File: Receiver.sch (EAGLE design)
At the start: 11 parts, among them IC1 25LC080P, J1 PIC_ICSP_6_PIN, U1 915MHz, U2 DS3234, X1 BU-SMA-V

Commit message: Updates
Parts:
- added BUTTON: TSW-106-02-S-S, con-samtec:TSW-106-02-S-S
- added C3, C4: (no value), resistor:C-EU050-025X075
- added PWR: 22-27-2021-02, con-molex:22-27-2021-02
- added SJ1: SOLDERJUMPERNO, SparkFun-Retired:SOLDERJUMPERNO
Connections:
- net N$10 renamed MOSI1
- net N$11 renamed MOSI2
- net N$6 renamed SCK1
- net N$7 renamed MISO1
- net N$8 renamed SCK2
- net N$9 renamed MISO2
- new net N$10: BUTTON-4.1, U$1.RD0
- new net N$11: BUTTON-6.1, U$1.RD3
- new net N$17: RA8875-8.S, U$1.RA4
- new net N$18: RA8875-4.S, U$1.RA0
- new net N$19: RA8875-10.S, U$1.RE1
- new net N$20: RA8875-11.S, U$1.RE2
- new net N$21: U$1.RD7, U1.DIO0
- new net N$22: J1.VCC, SJ1.1
- new net N$6: BUTTON-1.1, U$1.RC0
- new net N$7: BUTTON-2.1, U$1.RC1
- new net N$8: BUTTON-3.1, U$1.RC2
- new net N$9: BUTTON-5.1, U$1.RD1
- net +3V3: now also C3.1, C4.1, PWR-1.S, RA8875-1.S, SJ1.2; no longer J1.VCC
- net GND: now also C3.2, C4.2, PWR-2.S
- net N$12: now also U$1.RD6; no longer U$1.RD3
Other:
- moved on the sheet: BT1, IC1, U2

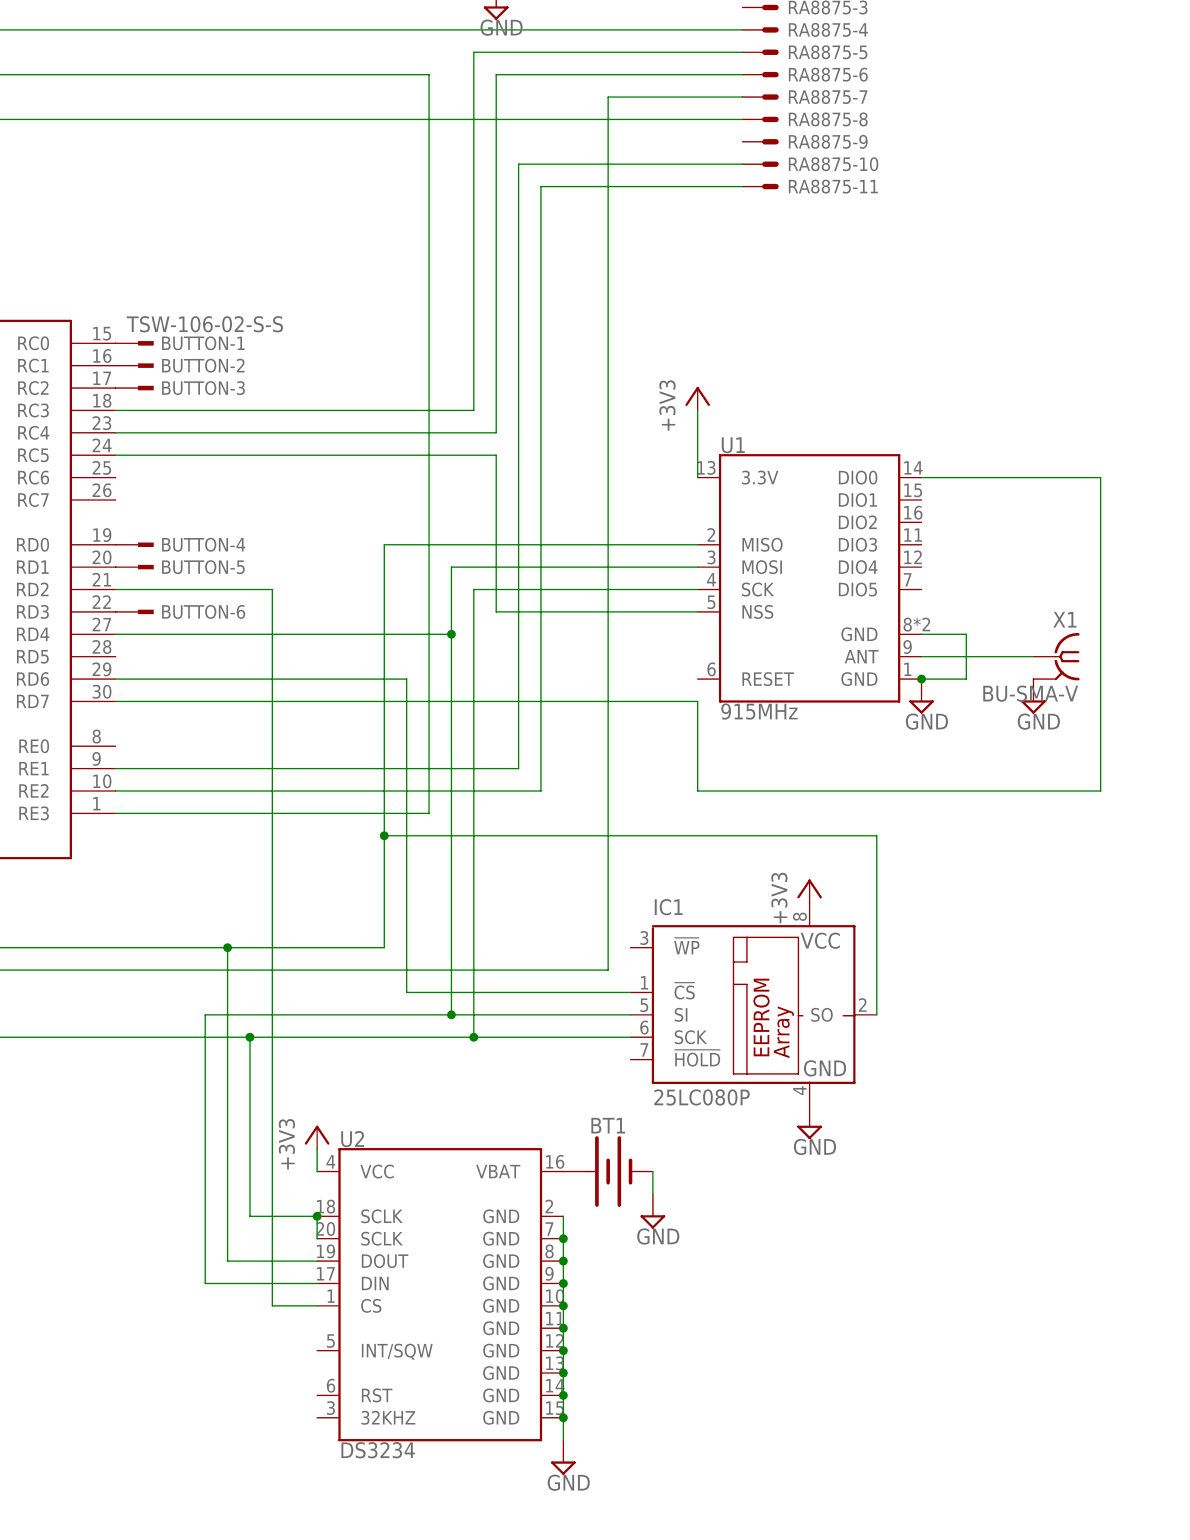
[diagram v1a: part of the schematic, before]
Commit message: Ordered sender PCB
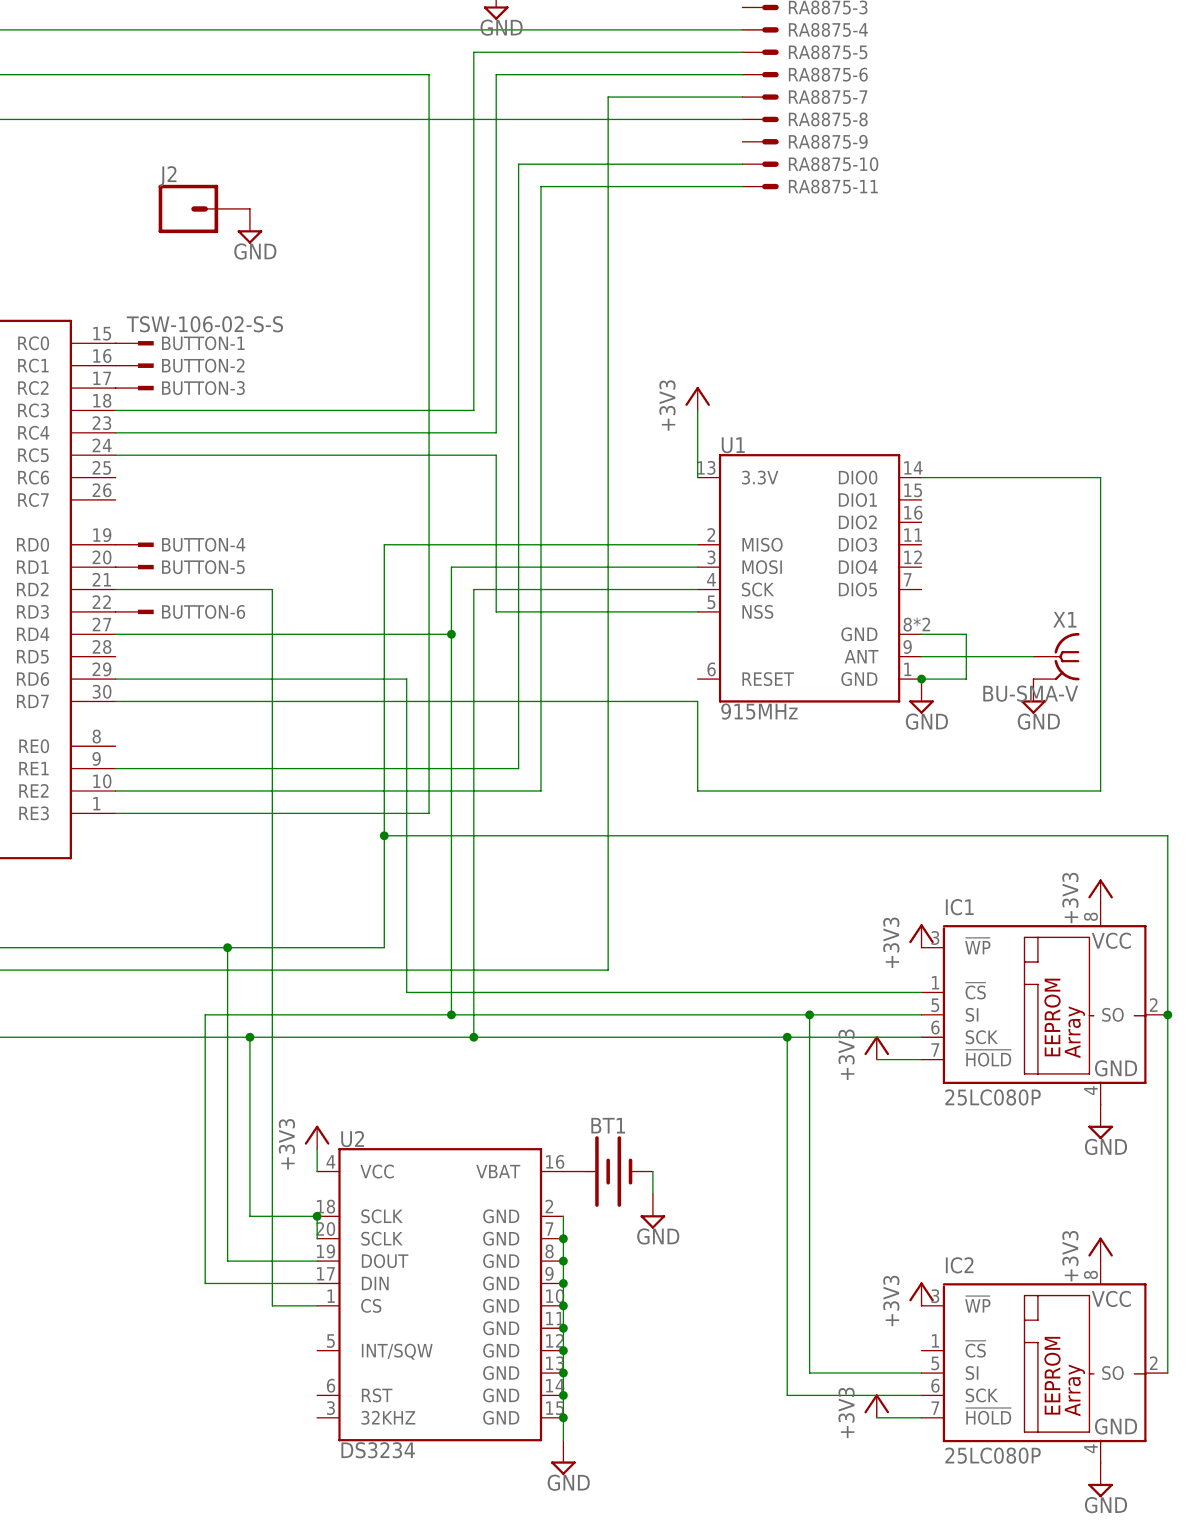
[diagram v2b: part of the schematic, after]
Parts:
- added IC2: 25LC080P, microchip:25LC080P
- added J2: (no value), SparkFun-Connectors:CONN_01
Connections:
- net +3V3: now also IC1.!HOLD, IC1.!WP, IC2.!HOLD, IC2.!WP, IC2.VCC
- net GND: now also IC2.GND, J2.1
- net MISO2: now also IC2.SO
- net MOSI2: now also IC2.SI
- net SCK2: now also IC2.SCK
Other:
- moved on the sheet: IC1
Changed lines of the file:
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@@
 <part name="C3" library="resistor" deviceset="C-EU" device="050-025X075"/>
 <part name="C4" library="resistor" deviceset="C-EU" device="050-025X075"/>
+<part name="IC2" library="microchip" deviceset="25*" device="P" technology="LC080"/>
+<part name="+3V8" library="supply1" deviceset="+3V3" device=""/>
+<part name="SUPPLY3" library="supply2" deviceset="GND" device=""/>
+<part name="+3V9" library="supply1" deviceset="+3V3" device=""/>
+<part name="+3V10" library="supply1" deviceset="+3V3" device=""/>
+<part name="+3V11" library="supply1" deviceset="+3V3" device=""/>
+<part name="+3V12" library="supply1" deviceset="+3V3" device=""/>
+<part name="J2" library="SparkFun-Connectors" deviceset="CONN_01" device=""/>
+<part name="SUPPLY6" library="supply2" deviceset="GND" device=""/>
 </parts>
 <sheets>
@@
 <instance part="RA8875" gate="-10" x="172.72" y="121.92"/>
 <instance part="RA8875" gate="-11" x="172.72" y="119.38"/>
-<instance part="IC1" gate="G$1" x="170.18" y="25.4"/>
-<instance part="SUPPLY7" gate="GND" x="177.8" y="12.7"/>
+<instance part="IC1" gate="G$1" x="203.2" y="25.4"/>
+<instance part="SUPPLY7" gate="GND" x="210.82" y="12.7"/>
 <instance part="SUPPLY8" gate="GND" x="190.5" y="60.96"/>
 <instance part="X1" gate="G$1" x="205.74" y="66.04" rot="MR0"/>
@@
 <instance part="+3V3" gate="G$1" x="78.74" y="111.76"/>
 <instance part="+3V4" gate="G$1" x="50.8" y="121.92"/>
-<instance part="+3V5" gate="G$1" x="177.8" y="40.64"/>
+<instance part="+3V5" gate="G$1" x="210.82" y="40.64"/>
 <instance part="+3V6" gate="G$1" x="162.56" y="147.32"/>
 <instance part="BUTTON" gate="-1" x="101.6" y="101.6"/>
@@
 <instance part="C3" gate="G$1" x="7.62" y="149.86"/>
 <instance part="C4" gate="G$1" x="-7.62" y="149.86"/>
+<instance part="IC2" gate="G$1" x="203.2" y="-15.24"/>
+<instance part="+3V8" gate="G$1" x="210.82" y="0"/>
+<instance part="SUPPLY3" gate="GND" x="210.82" y="-27.94"/>
+<instance part="+3V9" gate="G$1" x="190.5" y="35.56"/>
+<instance part="+3V10" gate="G$1" x="190.5" y="-5.08"/>
+<instance part="+3V11" gate="G$1" x="185.42" y="-17.78"/>
+<instance part="+3V12" gate="G$1" x="185.42" y="22.86"/>
+<instance part="J2" gate="G$1" x="106.68" y="116.84"/>
+<instance part="SUPPLY6" gate="GND" x="114.3" y="114.3"/>
 </instances>
 <busses>
@@
 <junction x="7.62" y="144.78"/>
 </segment>
+<segment>
+<pinref part="IC2" gate="G$1" pin="GND"/>
+<pinref part="SUPPLY3" gate="GND" pin="GND"/>
+</segment>
+<segment>
+<pinref part="J2" gate="G$1" pin="1"/>
+<pinref part="SUPPLY6" gate="GND" pin="GND"/>
+</segment>
 </net>
 <net name="N$1" class="0">
@@
 <wire x1="129.54" y1="78.74" x2="165.1" y2="78.74" width="0.1524" layer="91"/>
 <pinref part="IC1" gate="G$1" pin="SO"/>
-<wire x1="185.42" y1="25.4" x2="185.42" y2="45.72" width="0.1524" layer="91"/>
-<wire x1="185.42" y1="45.72" x2="129.54" y2="45.72" width="0.1524" layer="91"/>
+<wire x1="218.44" y1="25.4" x2="218.44" y2="45.72" width="0.1524" layer="91"/>
+<wire x1="218.44" y1="45.72" x2="129.54" y2="45.72" width="0.1524" layer="91"/>
 <junction x="129.54" y="45.72"/>
 <pinref part="U2" gate="G$1" pin="DOUT"/>
@@
 <wire x1="111.76" y1="-2.54" x2="111.76" y2="33.02" width="0.1524" layer="91"/>
 <junction x="111.76" y="33.02"/>
+<pinref part="IC2" gate="G$1" pin="SO"/>
+<wire x1="218.44" y1="25.4" x2="218.44" y2="-15.24" width="0.1524" layer="91"/>
+<junction x="218.44" y="25.4"/>
 </segment>
 </net>
@@
 <segment>
 <pinref part="IC1" gate="G$1" pin="SI"/>
-<wire x1="157.48" y1="25.4" x2="137.16" y2="25.4" width="0.1524" layer="91"/>
+<wire x1="190.5" y1="25.4" x2="177.8" y2="25.4" width="0.1524" layer="91"/>
 <pinref part="U1" gate="G$1" pin="MOSI"/>
+<wire x1="177.8" y1="25.4" x2="137.16" y2="25.4" width="0.1524" layer="91"/>
 <wire x1="137.16" y1="25.4" x2="137.16" y2="68.58" width="0.1524" layer="91"/>
 <wire x1="137.16" y1="68.58" x2="137.16" y2="76.2" width="0.1524" layer="91"/>
@@
 <wire x1="99.06" y1="68.58" x2="137.16" y2="68.58" width="0.1524" layer="91"/>
 <junction x="137.16" y="68.58"/>
+<wire x1="177.8" y1="25.4" x2="177.8" y2="-15.24" width="0.1524" layer="91"/>
+<junction x="177.8" y="25.4"/>
+<pinref part="IC2" gate="G$1" pin="SI"/>
+<wire x1="177.8" y1="-15.24" x2="190.5" y2="-15.24" width="0.1524" layer="91"/>
 </segment>
 </net>
@@
 <pinref part="SJ1" gate="1" pin="2"/>
 <wire x1="50.8" y1="119.38" x2="45.72" y2="119.38" width="0.1524" layer="91"/>
+</segment>
+<segment>
+<pinref part="IC2" gate="G$1" pin="VCC"/>
+<pinref part="+3V8" gate="G$1" pin="+3V3"/>
+</segment>
+<segment>
+<pinref part="IC1" gate="G$1" pin="!WP"/>
+<pinref part="+3V9" gate="G$1" pin="+3V3"/>
+</segment>
+<segment>
+<pinref part="IC2" gate="G$1" pin="!WP"/>
+<pinref part="+3V10" gate="G$1" pin="+3V3"/>
+</segment>
+<segment>
+<pinref part="IC1" gate="G$1" pin="!HOLD"/>
+<pinref part="+3V12" gate="G$1" pin="+3V3"/>
+<wire x1="190.5" y1="20.32" x2="185.42" y2="20.32" width="0.1524" layer="91"/>
+</segment>
+<segment>
+<pinref part="IC2" gate="G$1" pin="!HOLD"/>
+<pinref part="+3V11" gate="G$1" pin="+3V3"/>
+<wire x1="190.5" y1="-20.32" x2="185.42" y2="-20.32" width="0.1524" layer="91"/>
 </segment>
 </net>
@@
 <pinref part="U1" gate="G$1" pin="SCK"/>
 <wire x1="114.3" y1="22.86" x2="139.7" y2="22.86" width="0.1524" layer="91"/>
-<wire x1="139.7" y1="22.86" x2="157.48" y2="22.86" width="0.1524" layer="91"/>
+<wire x1="139.7" y1="22.86" x2="175.26" y2="22.86" width="0.1524" layer="91"/>
+<wire x1="175.26" y1="22.86" x2="190.5" y2="22.86" width="0.1524" layer="91"/>
 <wire x1="165.1" y1="73.66" x2="139.7" y2="73.66" width="0.1524" layer="91"/>
 <wire x1="139.7" y1="73.66" x2="139.7" y2="22.86" width="0.1524" layer="91"/>
@@
 <junction x="121.92" y="2.54"/>
 <junction x="114.3" y="22.86"/>
+<wire x1="175.26" y1="22.86" x2="175.26" y2="-17.78" width="0.1524" layer="91"/>
+<junction x="175.26" y="22.86"/>
+<pinref part="IC2" gate="G$1" pin="SCK"/>
+<wire x1="175.26" y1="-17.78" x2="190.5" y2="-17.78" width="0.1524" layer="91"/>
 </segment>
 </net>
@@
 <pinref part="IC1" gate="G$1" pin="!CS"/>
 <wire x1="132.08" y1="63.5" x2="132.08" y2="27.94" width="0.1524" layer="91"/>
-<wire x1="132.08" y1="27.94" x2="157.48" y2="27.94" width="0.1524" layer="91"/>
+<wire x1="132.08" y1="27.94" x2="190.5" y2="27.94" width="0.1524" layer="91"/>
 <pinref part="U$1" gate="G$1" pin="RD6"/>
 <wire x1="99.06" y1="63.5" x2="132.08" y2="63.5" width="0.1524" layer="91"/>

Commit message: Updated receiver PCB
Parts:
- removed J1: PIC_ICSP_6_PIN, SparkFun-Connectors:PIC_ICSP_6_PIN
- added IC3: (no value), v-reg:78XXS
- added PWR1: 22-27-2021-02, con-molex:22-27-2021-02
- added R1, R2, R3, R4, R5, R6: (no value), resistor:R-US_M1206
- added X2: 53047-05, con-molex:53047-05
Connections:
- new net N$23: IC2.!CS, U$1.RC6
- new net N$24: IC3.IN, PWR1-1.S
- net +3V3: now also IC3.OUT, R1.2, R2.2, R3.2, R4.2, R5.2, R6.2
- net GND: now also IC3.GND, PWR1-2.S, X2-3.S; no longer J1.GND
- net N$1: now also X2-4.S; no longer J1.PGD
- net N$10: now also R4.1
- net N$11: now also R6.1
- net N$2: now also X2-5.S; no longer J1.PGC
- net N$22: now also X2-2.S; no longer J1.VCC
- net N$3: now also X2-1.S; no longer J1.VPP
- net N$6: now also R1.1
- net N$7: now also R2.1
- net N$8: now also R3.1
- net N$9: now also R5.1
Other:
- moved on the sheet: BUTTON-1, BUTTON-2, BUTTON-3, BUTTON-4, BUTTON-5, BUTTON-6

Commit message: Receiver board r2
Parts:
- removed BT1: (no value), SparkFun-Batteries:BATTERY-20MM_SMD
- removed BUTTON: TSW-106-02-S-S, con-samtec:TSW-106-02-S-S
- removed IC1, IC2: 25LC080P, microchip:25LC080P
- removed IC3: (no value), v-reg:78XXS
- removed PWR1: 22-27-2021-02, con-molex:22-27-2021-02
- removed Q1: (no value), crystal:CRYSTALHC49U-V
- removed R2, R3, R4, R5, R6: (no value), resistor:R-US_M1206
- removed SJ1: SOLDERJUMPERNO, SparkFun-Retired:SOLDERJUMPERNO
- removed U$1: PIC18F47K40, microchip:PIC18F47K40
- added C5, C6: (no value), resistor:C-EUC1206
- added C7: 0.1uF, resistor:C-EUC1206
- added I2C-DBG: (no value), SparkFun-Connectors:CONN_03
- added J1: SD_CARD_SOCKET, SparkFun-Connectors:SD_CARD_SOCKET
- added RA8875-DBG: (no value), SparkFun-Connectors:CONN_09
- added SPI2-DBG: (no value), SparkFun-Connectors:CONN_08"
- added TP3V3, TPCLKOUT, TPSQW, TPVBUS: TPB2,54, testpad:TPB2,54
- added U$3: (no value), adafruit:CR1220SMT
- added U4: FT232RL, SparkFun-IC-Comms:FT232RL-BASICSSOP
- added U5: DS1374C, FRC696:DS1374C
- added U6: +12v, SparkFun-IC-Power:V_REG_78XX7812
- added UARTDBG: 53047-03, con-molex:53047-03
- C1: value (none) -> 0.1uF
- C2: value (none) -> 1uF
- C3: value (none) -> 0.1uF; device resistor:C-EU050-025X075 -> resistor:C-EUC1206
- C4: value (none) -> 1uF; device resistor:C-EU050-025X075 -> resistor:C-EUC1206
- J2: device SparkFun-Connectors:CONN_01 -> SparkFun-Connectors:USB_MICRO-B_FEMALE-SMT
- PWR: value 22-27-2021-02 -> 53261-02; device con-molex:22-27-2021-02 -> con-molex:53261-02
- R1: value (none) -> 10k; device resistor:R-US_M1206 -> resistor:R-US_R1206
- RA8875: value C-GRID-11-70543 -> C-GRID-10-70543; device con-molex:C-GRID-11-70543 -> con-molex:C-GRID-10-70543
- U1: value 915MHz -> PIC18F47Q84; device SparkFun-RF:RFM69HCW-915 -> FRC696:PIC18F47Q84
- U2: value DS3234 -> 915MHz; device SparkFun-Clocks:DS3234 -> SparkFun-RF:RFM69HCW-915
- X2: value 53047-05 -> PIC-PROG047; device con-molex:53047-05 -> FRC696:PIC-PROG047
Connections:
- removed net N$14: BT1.+, U2.VBAT
- removed net N$15: U$1.RC5, U1.NSS
- removed net N$16: U$1.RD2, U2.CS
- removed net N$17: RA8875-8.S, U$1.RA4
- removed net N$18: RA8875-4.S, U$1.RA0
- removed net N$19: RA8875-10.S, U$1.RE1
- removed net N$20: RA8875-11.S, U$1.RE2
- removed net N$21: U$1.RD7, U1.DIO0
- removed net N$22: SJ1.1, X2-2.S
- removed net N$23: IC2.!CS, U$1.RC6
- removed net N$24: IC3.IN, PWR1-1.S
- new net CLK_RST: U5.!RST
- new net RA8875-CS: RA8875-7.S, RA8875-DBG.6, U1.RD7
- new net RA8875-INT: RA8875-10.S, RA8875-DBG.9, U1.RC4
- new net RA8875-LITE: RA8875-3.S, RA8875-DBG.2, U1.RD0
- new net RA8875-RST: RA8875-8.S, RA8875-DBG.7, U1.RD6
- new net RA8875-WAIT: RA8875-9.S, RA8875-DBG.8, U1.RD5
- new net RF-CS: SPI2-DBG.5, U1.RC5, U2.NSS
- new net RF-DIO0: SPI2-DBG.7, U1.RC7, U2.DIO0
- new net RF-RST: SPI2-DBG.6, U1.RC6, U2.RESET
- new net SCL: I2C-DBG.2, U1.RB5, U5.SCL
- new net SD-CS: J1.CD/DAT3, SPI2-DBG.8, U1.RD4
- new net SDA: I2C-DBG.3, U1.RB4, U5.SDA
- new net UARTRX: U1.RB2, U4.TXD, UARTDBG-3.S
- new net UARTTX: U1.RB1, U4.RXD, UARTDBG-2.S
- net +3V3: now also C5.1, C6.1, J1.VDD, TP3V3.TP, U1.VDD@1, U1.VDD@2, U2.3.3V, U4.VCC, U4.VCCIO, U5.VCC, U6.OUT, X2VDD.S; no longer IC1.!HOLD, IC1.!WP, IC1.VCC, IC2.!HOLD, IC2.!WP, IC2.VCC, IC3.OUT, PWR-1.S, R2.2, R3.2, R4.2, R5.2, R6.2, SJ1.2, U$1.VDD@1, U$1.VDD@2, U1.3.3V, U2.VCC
- net GND: now also C1.2, C2.2, C5.2, C6.2, C7.2, I2C-DBG.1, J1.SH@1, J1.SH@2, J1.VSS1, J1.VSS2, J2.GND, RA8875-DBG.1, SPI2-DBG.1, U$3.-, U1.VSS@1, U1.VSS@2, U2.GND@1, U4.AGND, U4.GND1, U4.GND2, U4.GND3, U4.TEST, U5.GND, U6.GND, UARTDBG-1.S, X2VSS.S; no longer BT1.-, C1.1, C2.1, IC1.GND, IC2.GND, IC3.GND, J2.1, PWR1-2.S, U$1.VSS@1, U$1.VSS@2, U1.GND@1, U1.GND@2, U2.GND, U2.GND@10, U2.GND@11, U2.GND@12, U2.GND@13, U2.GND@14, U2.GND@7, U2.GND@8, U2.GND@9, X2-3.S
- net MISO1: now also RA8875-5.S, RA8875-DBG.4, U1.RC2; no longer RA8875-6.S, U$1.RC4
- net MISO2: now also J1.DAT0, SPI2-DBG.2, U1.RD2, U2.MISO; no longer IC1.SO, IC2.SO, U$1.RB2, U1.MISO, U2.DOUT
- net MOSI1: now also RA8875-6.S, RA8875-DBG.5, U1.RC1; no longer RA8875-7.S, U$1.RB3
- net MOSI2: now also J1.CMD, SPI2-DBG.3, U1.RD3, U2.MOSI; no longer IC1.SI, IC2.SI, U$1.RD4, U1.MOSI, U2.DIN
- net N$1: now also U1.RB6/PGC, X2PGC.S; no longer U$1.RB7, X2-4.S
- net N$10: now also U$3.+, U$3.+1, U5.VBACKUP; no longer BUTTON-4.1, R4.1, U$1.RD0
- net N$11: now also TPSQW.TP, U5.SQW; no longer BUTTON-6.1, R6.1, U$1.RD3
- net N$12: now also TPCLKOUT.TP, U1.RA6/CLKOUT; no longer IC1.!CS, U$1.RD6
- net N$13: now also U2.ANT; no longer U1.ANT
- net N$2: now also U1.RB7/PGD, X2PGD.S; no longer U$1.RB6, X2-5.S
- net N$3: now also R1.1, U1.RE3/!MCLR, X2!MCLR.S; no longer U$1.RE3, X2-1.S
- net N$4: now also C1.1, C2.1, PWR-1.S, U6.IN; no longer C1.2, Q1.2, U$1.RA6
- net N$5: now also J2.VBUS, TPVBUS.TP; no longer C2.2, Q1.1, U$1.RA7
- net N$6: now also C7.1, U4.3V3OUT; no longer BUTTON-1.1, R1.1, U$1.RC0
- net N$7: now also J2.D-, U4.USBDM; no longer BUTTON-2.1, R2.1, U$1.RC1
- net N$8: now also J2.D+, U4.USBDP; no longer BUTTON-3.1, R3.1, U$1.RC2
- net N$9: now also U1.RC0; no longer BUTTON-5.1, R5.1, U$1.RD1
- net SCK1: now also RA8875-4.S, RA8875-DBG.3, U1.RC3; no longer RA8875-5.S, U$1.RC3
- net SCK2: now also J1.CLK, SPI2-DBG.4, U1.RD1, U2.SCK; no longer IC1.SCK, IC2.SCK, U$1.RB1, U1.SCK, U2.SCLK@18, U2.SCLK@20
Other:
- moved on the sheet: C1, C2, C3, C4, PWR-1, PWR-2, R1, RA8875-10, RA8875-3, RA8875-4, RA8875-5, RA8875-6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
